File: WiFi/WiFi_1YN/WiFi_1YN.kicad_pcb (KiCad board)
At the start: 4 copper layers, 31.6 x 14.9 mm, 9 parts, among them J1 ANT, J2 DF40C-20DP-0.4V_51_, J3 DF40C-20DP-0.4V_51_, U1 LBEE5KL1YN-814, Y1 ECS-327MVATX-3-CN-TR3

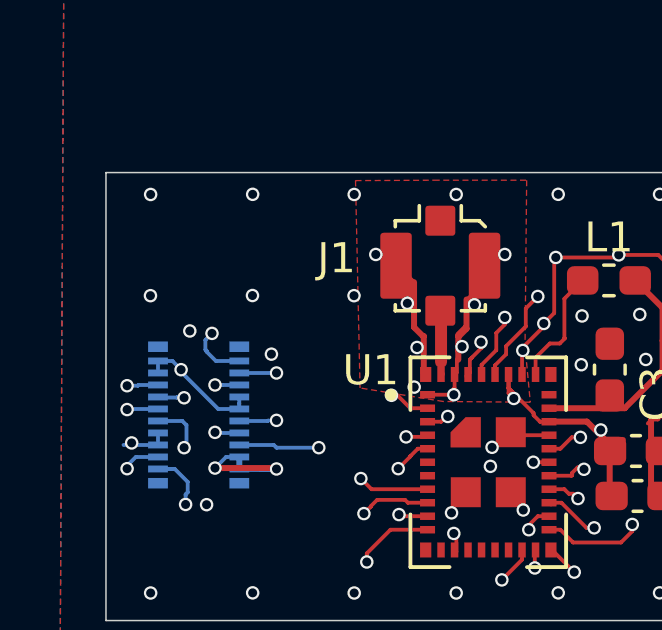
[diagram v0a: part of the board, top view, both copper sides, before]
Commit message: fix the rts/cts line being swapped and missing led0 connection (PWM0)
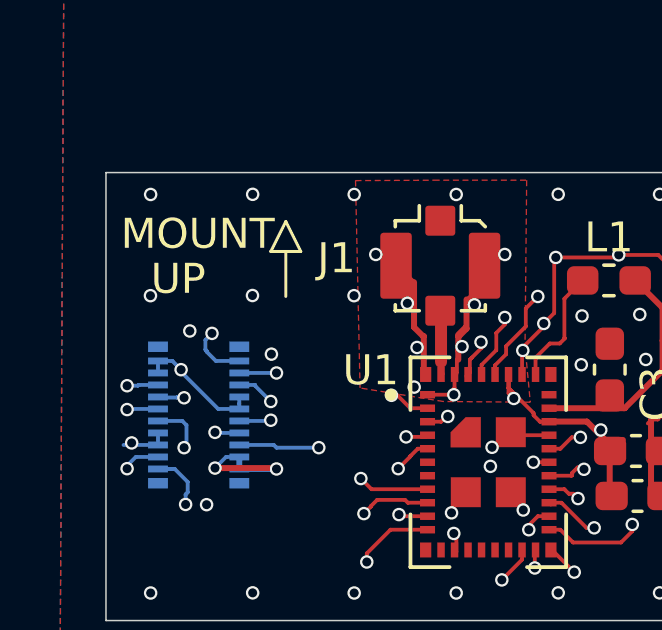
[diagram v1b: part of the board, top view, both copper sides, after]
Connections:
- J3 pad 15: /BT_UART_RTS -> /BT_UART_CTS
- J3 pad 9: /BT_UART_CTS -> /BT_UART_RTS
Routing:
- net /BT_UART_RTS: track 9.26 -> 7.34 mm
- net /BT_UART_CTS: track 6.40 -> 7.03 mm
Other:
- board text added: "MOUNT"
- board text added: "UP"
